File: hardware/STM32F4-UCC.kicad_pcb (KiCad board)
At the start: 2 copper layers, 120 parts, among them J1 DB15, J2 STM32F4_Discovery_Header, J3 RJ45-TRANSFO_W, Q1 IRLML6402, SW1 BT1, SW2 BT2, SW3 BT3, SW4 BT4, U1 PLCC4, U2 FT230X, U3 DP83848C, U4 MSP1825S-3302E, U5 microSD, X1 50Mhz

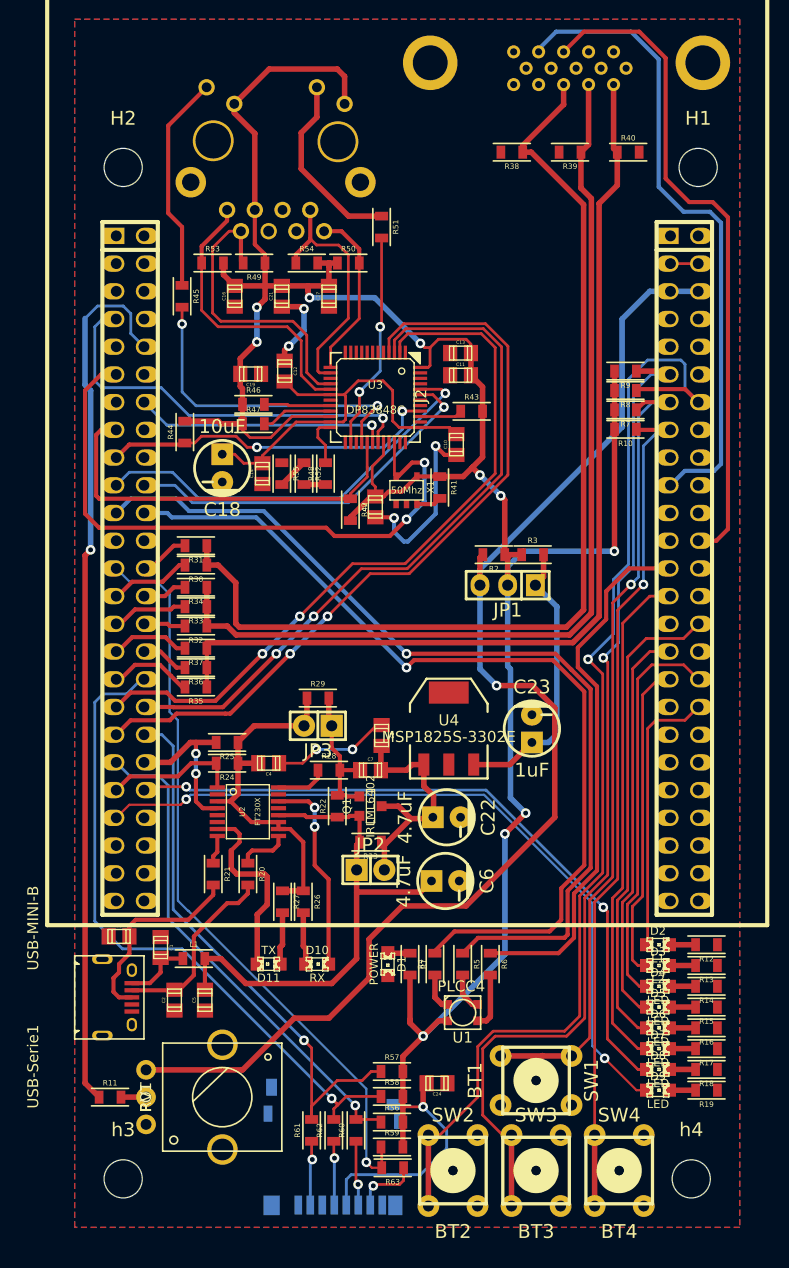
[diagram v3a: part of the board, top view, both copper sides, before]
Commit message: Se reRouteo con clearance 12 en general
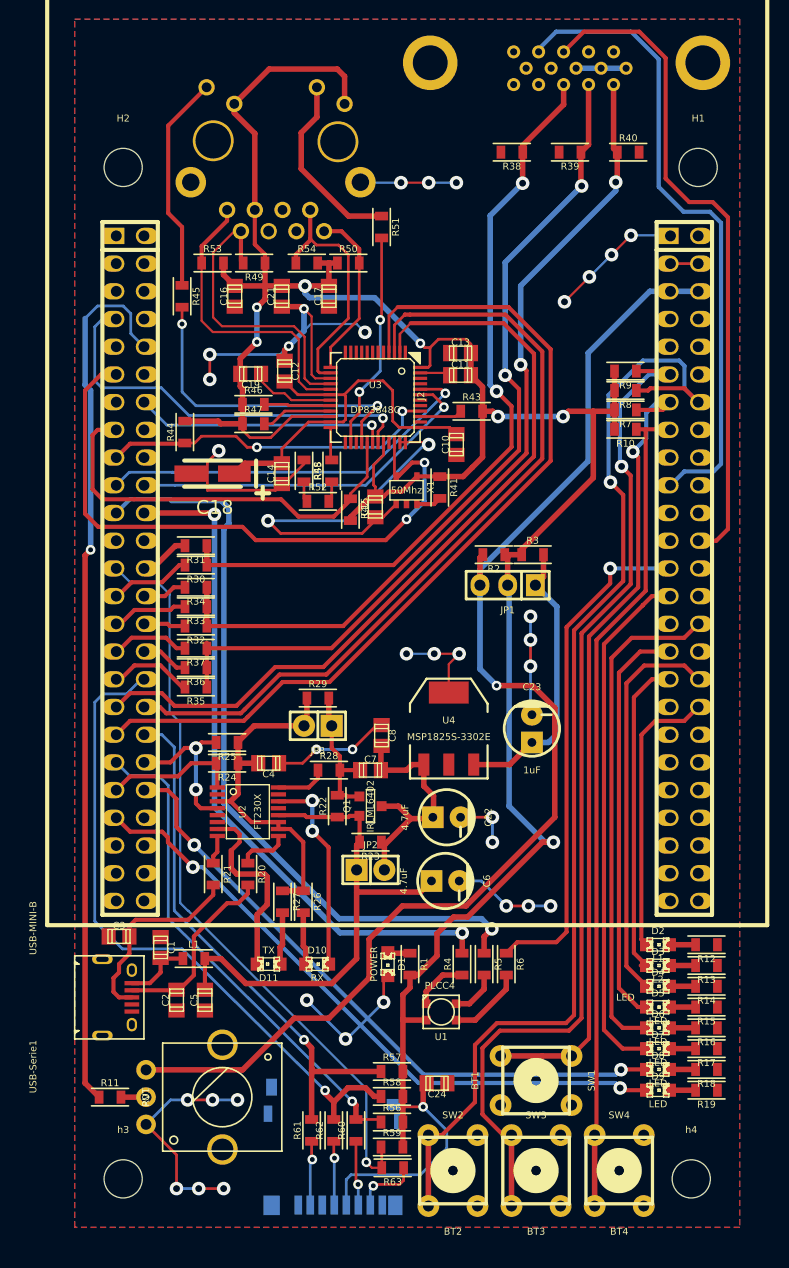
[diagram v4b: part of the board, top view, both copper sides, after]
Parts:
- C18: value 10uF -> 10uF (tantalio); footprint Capacitors_ThroughHole:Capacitor5x11RM2.5 -> Capacitors_Tantalum_SMD:TantalC_SizeA_EIA-3216_HandSoldering
- moved R52 2.84 mm to (76.9, 88.4), turned to 0 degrees
- moved R4 2.48 mm to (90.1, 130.8)
- moved R55 2.05 mm to (75.6, 85.6)
- moved U1 1.97 mm to (88.2, 135.2)
- moved R5 1.97 mm to (92.1, 130.8)
- moved C14 1.78 mm to (73.6, 85.9)
- moved R6 1.46 mm to (94.2, 130.8)
- moved C18 1.02 mm to (67.2, 85.9)
- moved R48 0.63 mm to (78.2, 85.6)
- moved C2 0.19 mm to (63.9, 134.1)
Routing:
- net GND: track 35.2 -> 195.0 mm, vias 6 -> 37
- net Net-(J1-Pad3): track 94.0 -> 71.0 mm, vias 0 -> 2
- net /PB0: track 82.5 -> 62.7 mm, vias 1 -> 2
- net /PB1: track 85.0 -> 70.3 mm
- net Net-(J1-Pad2): track 89.1 -> 76.1 mm, vias 0 -> 2
- net Net-(J1-Pad1): track 90.6 -> 78.6 mm, vias 0 -> 2
- net /Ethernet/TXD1: track 71.2 -> 80.6 mm, vias 2 -> 0
- net /PD11: track 68.9 -> 59.7 mm
- net /Ethernet/TXD0: track 65.8 -> 74.5 mm, vias 2 -> 0
- net +3.3V: track 259.2 -> 251.3 mm, vias 11 -> 8
- net /Ethernet/TX_EN: track 66.4 -> 73.8 mm, vias 2 -> 0
- net /PD10: track 64.3 -> 59.6 mm
- net /PB4: track 49.5 -> 46.8 mm, vias 0 -> 1
- net /SD-Card/Dat0/MISO: track 51.5 -> 49.2 mm
- net /PD6: track 43.7 -> 45.8 mm
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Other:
- net class Alimentacion: clearance 0.2032 -> 0.3048; via_dia 0.889 -> 1.2446; via_drill 0.635 -> 0.889
- net class Default: clearance 0.2032 -> 0.3048; via_dia 0.889 -> 1.2446; via_drill 0.635 -> 0.889
- rule trace_clearance: 0.2032 -> 0.3048

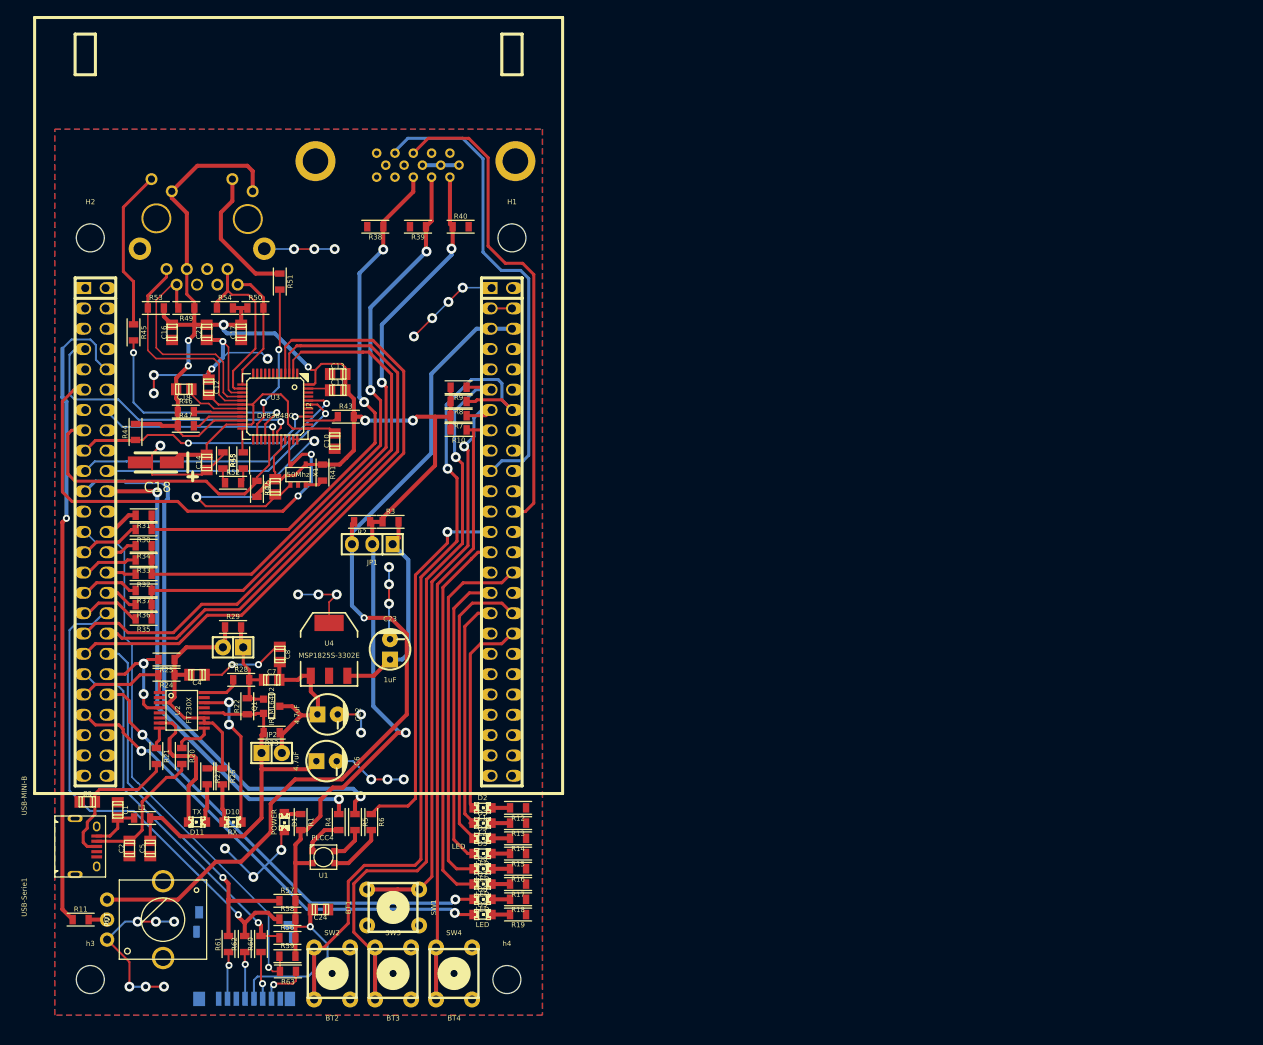
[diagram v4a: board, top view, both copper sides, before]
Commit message: Placa terminada, serigrafia verificada, logos agregados
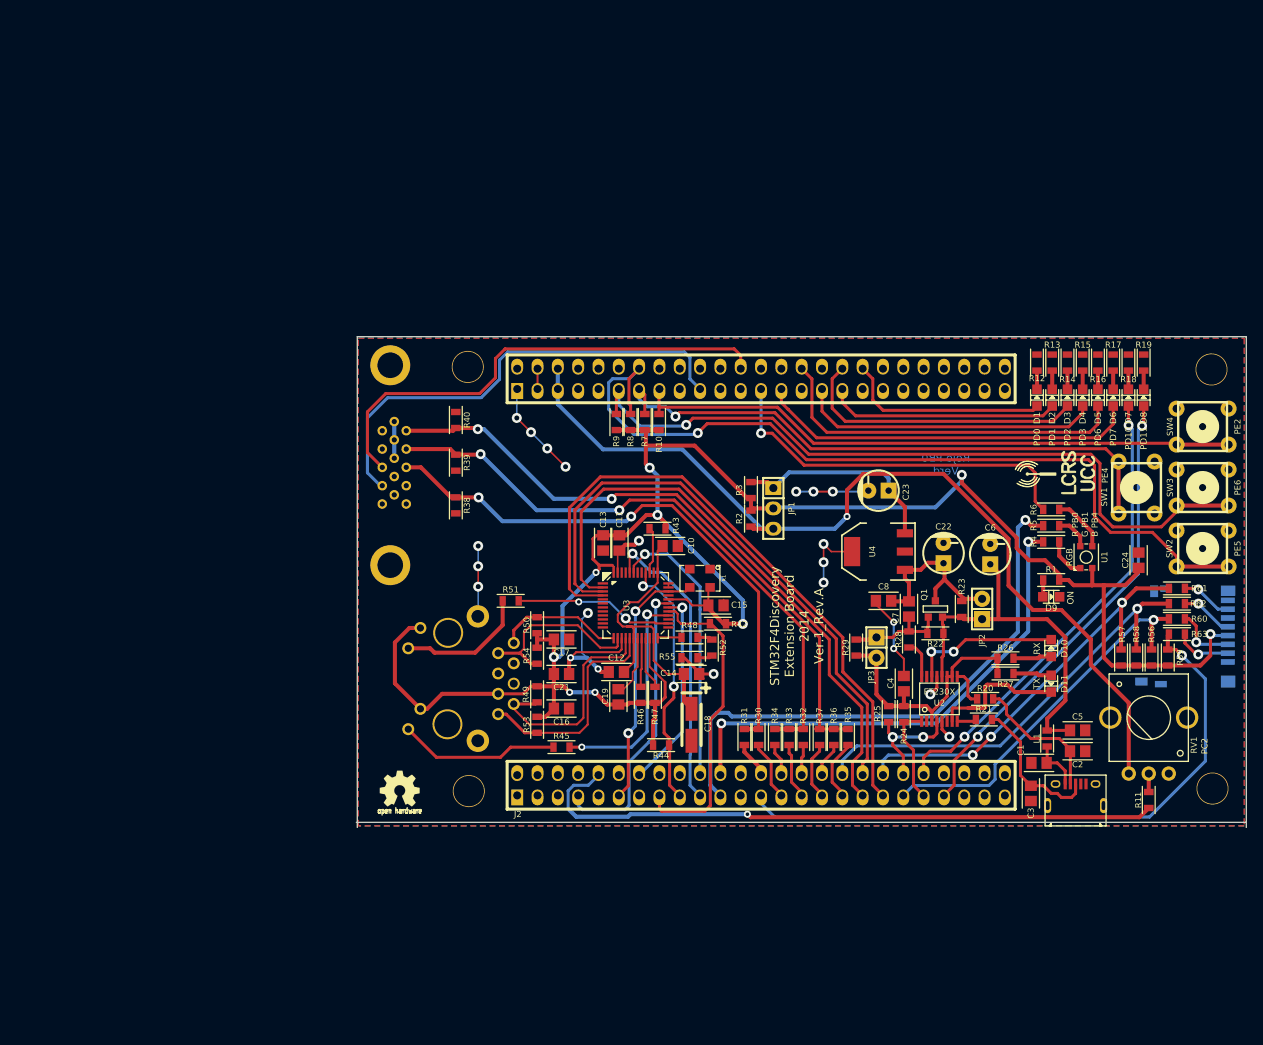
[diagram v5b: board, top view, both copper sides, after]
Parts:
- removed H1, H2, h3, h4: MountingHole_3-5mm_RevA_Date21Jun2010, Mounting_Holes:MountingHole_3-5mm
- removed R41: 1k, Resistors_SMD:R_0805
- added G***: LOGO, w_Connectors:LOGO_UCC, F.Cu at (179.6, 87.1)
- added G***: LOGO, w_logo:Logo_silk_OSHW_6x6mm, F.Cu at (97.7, 126.6)
- added MH: MountingHole_3-5mm_RevA_Date21Jun2010, Mounting_Holes:MountingHole_3-5mm, F.Cu at (199.2, 74.2)
- added MH: MountingHole_3-5mm_RevA_Date21Jun2010, Mounting_Holes:MountingHole_3-5mm, F.Cu at (199.3, 126.6)
- added MH: MountingHole_3-5mm_RevA_Date21Jun2010, Mounting_Holes:MountingHole_3-5mm, F.Cu at (106.2, 73.9)
- added MH: MountingHole_3-5mm_RevA_Date21Jun2010, Mounting_Holes:MountingHole_3-5mm, F.Cu at (106.4, 126.9)
- C1, C10, C11, C12, C13, C14, C15, C16, C17, C19, C2, C21, C24, C3, C4, C5, C7, C8: footprint Capacitors_SMD:c_0805 -> w_Connectors:c_0805
- D1: value POWER -> PD0; footprint LEDs:LED-0805 -> w_Connectors:Led_0805
- D10, D11: footprint LEDs:LED-0805 -> w_Connectors:Led_0805
- D2: value L1 -> PD1; footprint LEDs:LED-0805 -> w_Connectors:Led_0805
- D3: value L2 -> PD2; footprint LEDs:LED-0805 -> w_Connectors:Led_0805
- D4: value LED -> PD3; footprint LEDs:LED-0805 -> w_Connectors:Led_0805
- D5: value LED -> PD6; footprint LEDs:LED-0805 -> w_Connectors:Led_0805
- D6: value LED -> PD7; footprint LEDs:LED-0805 -> w_Connectors:Led_0805
- D7: value LED -> PD10; footprint LEDs:LED-0805 -> w_Connectors:Led_0805
- D8: value LED -> PD11; footprint LEDs:LED-0805 -> w_Connectors:Led_0805
- D9: value LED -> ON; footprint LEDs:LED-0805 -> w_Connectors:Led_0805
- RV1: value POT -> PC2
- SW1: value BT1 -> PE4
- SW2: value BT2 -> PE5
- SW3: value BT3 -> PE6
- SW4: value BT4 -> PE2
- U1: value PLCC4 -> RGB
- U3: footprint w_smd_lqfp:lqfp48 -> w_Connectors:lqfp48
- U4: value MSP1825S-3302E -> MCP1825S-3302E
- U5: footprint w_Connectors:microSD -> microSD
- X1: footprint SMD_Packages:SOT-23-5 -> w_Connectors:crystal_fa128
- moved R11 134.3 mm to (191.4, 128.0), turned to 90 degrees
- moved RV1 131.5 mm to (191.4, 124.7), turned to 0 degrees
- moved U5 127.3 mm to (200.4, 103.1), turned to 270 degrees
- moved R61 126.6 mm to (194.9, 101.6), turned to 180 degrees
- moved USB-Serie1 125.2 mm to (182.2, 128.7), turned to 0 degrees
- moved R62 124.0 mm to (194.9, 103.5), turned to 180 degrees
- moved R60 121.5 mm to (194.9, 105.4), turned to 180 degrees
- moved SW2 121.1 mm to (198.1, 96.6), turned to 90 degrees
- moved C2 119.1 mm to (182.5, 122.0), turned to 180 degrees
- moved R63 118.9 mm to (194.9, 107.3)
- moved SW3 118.0 mm to (198.1, 89.0), turned to 90 degrees
- moved C3 118.0 mm to (176.6, 127.2), turned to 90 degrees
- moved C5 116.9 mm to (182.5, 119.3), turned to 180 degrees
- moved R59 116.2 mm to (193.7, 110.2), turned to 270 degrees
- moved SW4 115.9 mm to (198.1, 81.4), turned to 90 degrees
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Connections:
- D1 pad 1: Net-(D1-Pad1) -> /PD0
- D1 pad 2: GND -> Net-(D1-Pad2)
- D2 pad 1: /PD0 -> /PD1
- D3 pad 1: /PD1 -> /PD2
- D4 pad 1: /PD2 -> /PD3
- D5 pad 1: /PD3 -> /PD6
- D6 pad 1: /PD6 -> /PD7
- D7 pad 1: /PD7 -> /PD10
- D8 pad 1: /PD10 -> /PD11
- D9 pad 1: /PD11 -> Net-(D9-Pad1)
- D9 pad 2: Net-(D9-Pad2) -> GND
- R1 pad 1: Net-(D1-Pad1) -> Net-(D9-Pad1)
- R12 pad 2: Net-(D2-Pad2) -> Net-(D1-Pad2)
- R13 pad 2: Net-(D3-Pad2) -> Net-(D2-Pad2)
- R14 pad 2: Net-(D4-Pad2) -> Net-(D3-Pad2)
- R15 pad 2: Net-(D5-Pad2) -> Net-(D4-Pad2)
- R16 pad 2: Net-(D6-Pad2) -> Net-(D5-Pad2)
- R17 pad 2: Net-(D7-Pad2) -> Net-(D6-Pad2)
- R18 pad 2: Net-(D8-Pad2) -> Net-(D7-Pad2)
- R19 pad 2: Net-(D9-Pad2) -> Net-(D8-Pad2)
- X1 pad 1: GND -> (no net)
- X1 pad 2: (no net) -> GND
- X1 pad 3: Net-(R41-Pad2) -> /Ethernet/OSCIN
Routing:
- net GND: track 195.0 -> 104.4 mm, vias 37 -> 22
- net /Ethernet/OSCIN: track 58.2 -> 32.0 mm
- net +3.3V: track 251.3 -> 262.7 mm, vias 8 -> 9
- net /SD-Card/Dat3/CS: track 69.0 -> 78.6 mm
- net /SD-Card/CLK/SCK: track 61.1 -> 56.2 mm
- net /SD-Card/Dat0/MISO: track 49.2 -> 52.6 mm, vias 1 -> 3
- net Net-(D9-Pad2): track 2.40 -> 0.00 mm
- net Net-(D1-Pad2): track 0.00 -> 2.40 mm
- net Net-(R41-Pad2): track 2.31 -> 0.00 mm
- net Net-(R45-Pad2): track 30.1 -> 27.9 mm
- net Net-(D9-Pad1): track 0.00 -> 2.05 mm
- net Net-(D1-Pad1): track 2.05 -> 0.00 mm
- net Net-(R60-Pad1): track 5.93 -> 7.88 mm
- net Net-(R43-Pad1): track 3.93 -> 5.84 mm
- net /Ethernet/RXD0: track 33.2 -> 35.0 mm
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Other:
- board outline added: 111.3 x 61.3 mm
- net class Alimentacion: clearance 0.3048 -> 0.2032
- net class Default: clearance 0.3048 -> 0.2032
- rule trace_clearance: 0.3048 -> 0.2032
- board text added: "R PB0 G PB1 B PB4"
- board text added: "Rojo PB0 Verd"
- board text added: "STM32F4Discovery Extension Board 2014 Ver.1_Rev.A"

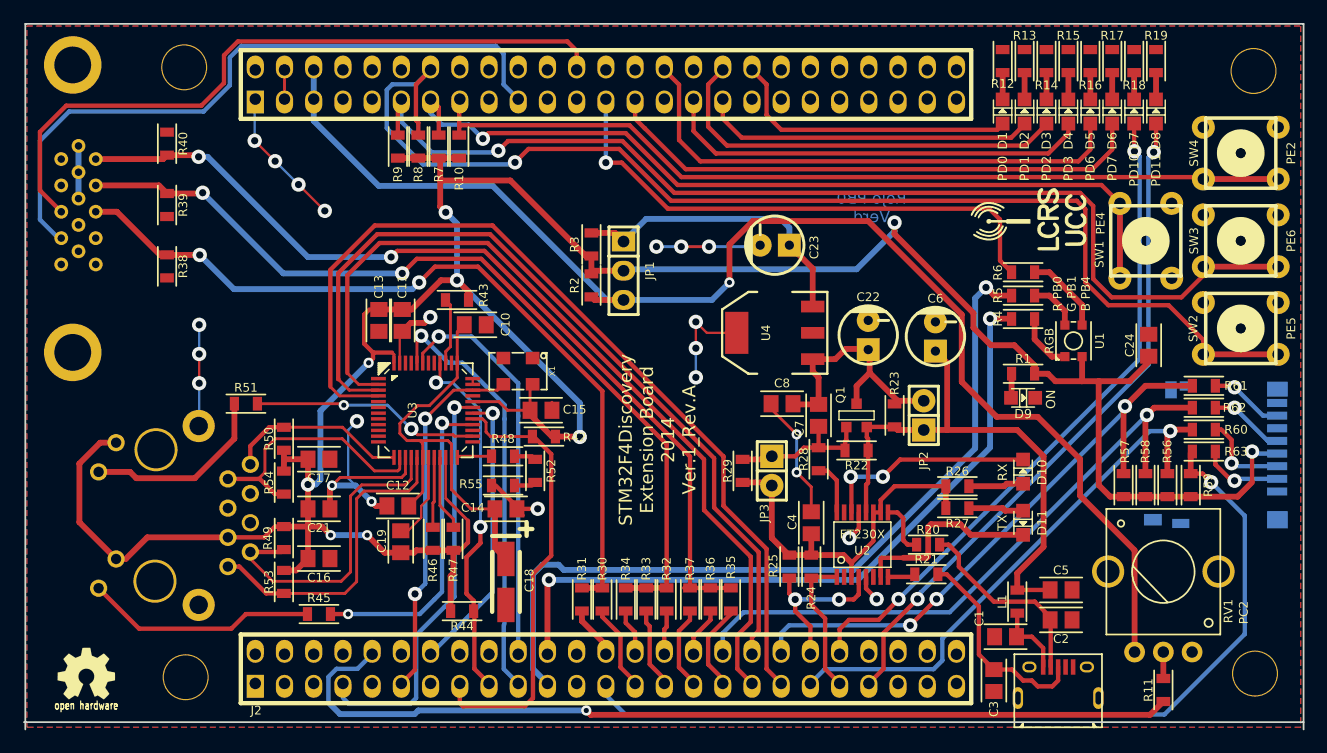
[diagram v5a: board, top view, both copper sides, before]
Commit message: Se agregan salidas de archivos en PDF y se realizan algunos cambios
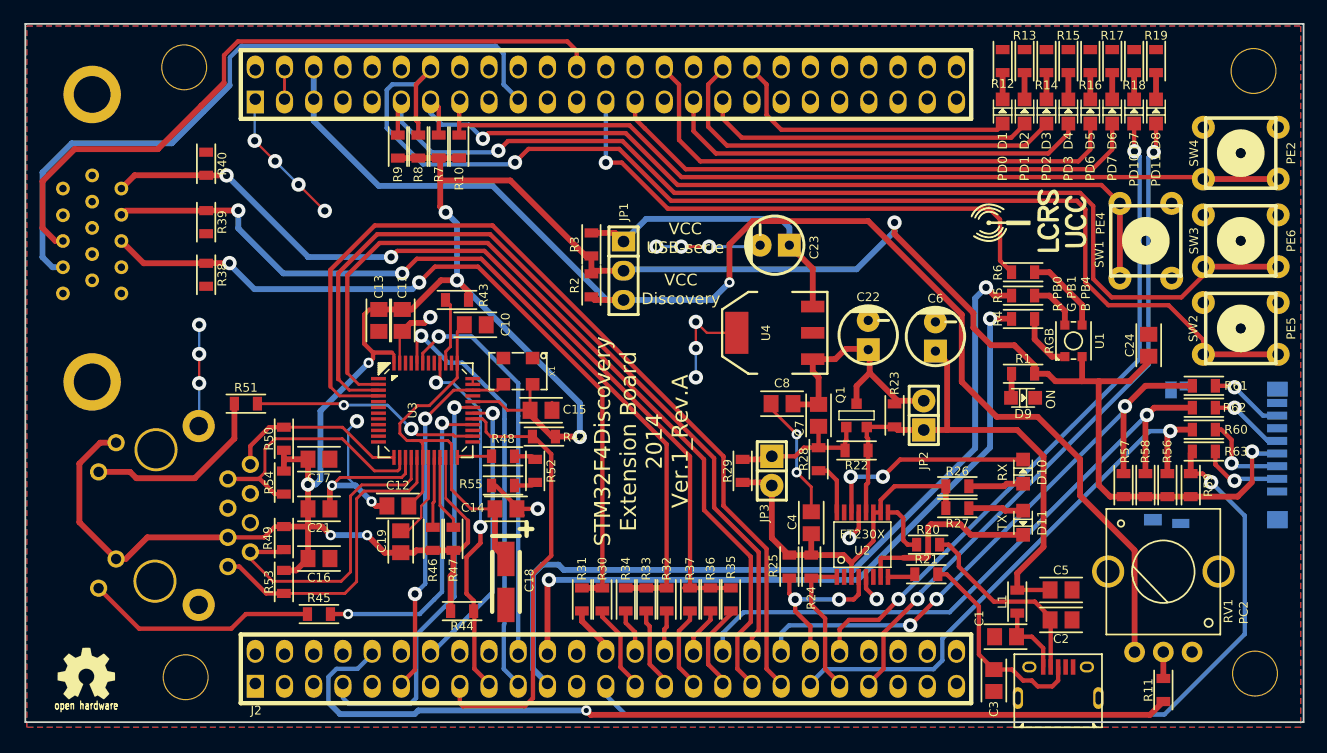
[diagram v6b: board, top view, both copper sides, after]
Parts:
- J1: footprint w_conn_pc:DB_15F-VGA -> w_Connectors:DB_15F-VGA
- U5: footprint microSD -> w_Connectors:microSD
- moved J1 5.06 mm to (98.2, 83.3)
- moved R40 3.82 mm to (108.1, 82.3)
- moved R39 3.71 mm to (108.1, 87.4)
- moved R38 3.47 mm to (108.1, 91.9)
- moved G*** 0.13 mm to (179.6, 87.2)
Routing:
- net GND: track 104.4 -> 99.9 mm
- net Net-(J1-Pad3): track 71.0 -> 67.8 mm
- net Net-(J1-Pad1): track 78.6 -> 76.0 mm
- net Net-(J1-Pad2): track 76.1 -> 74.0 mm
- net /VGA/VGA_VS: track 59.3 -> 60.3 mm
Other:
- board size 111.3 x 61.3 mm -> 111.1 x 60.7 mm
- board text added: "VCC Discovery"
- board text added: "VCC USB-serie"
- board text removed: "Rojo PB0 Verd"
